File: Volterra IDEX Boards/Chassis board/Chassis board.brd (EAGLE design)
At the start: 102.2 x 54 mm, 29 parts, among them K1 FFC/FPC/34PIN/1MMPITCH/TOPLOCK, K2 FFC/FPC/34PIN/1MMPITCH/TOPLOCK, K3 FFC/FPC/34PIN/1MMPITCH/TOPLOCK, X1 JST-XH-02-PIN-LONG-PAD

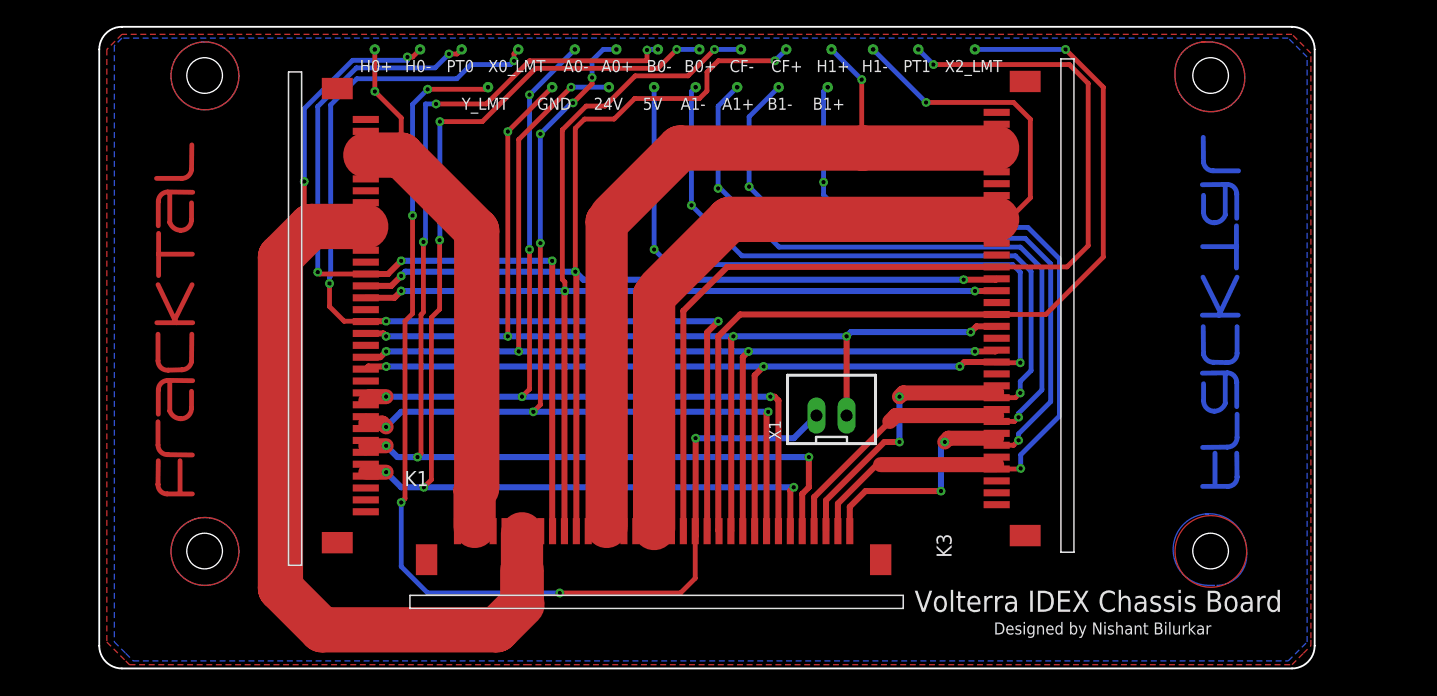
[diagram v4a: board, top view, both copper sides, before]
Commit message: Updated Chassis Board mount holes and re-routing
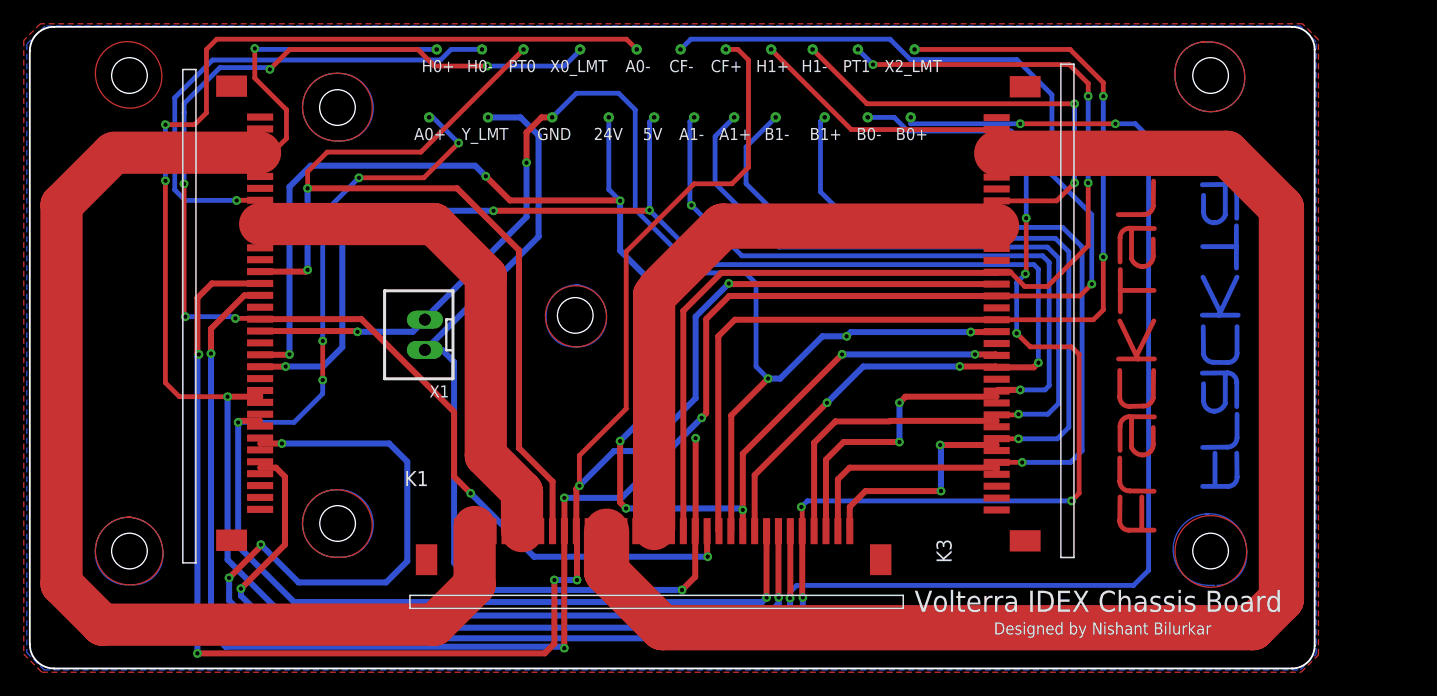
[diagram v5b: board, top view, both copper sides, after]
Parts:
- moved U$2 81.0 mm to (96.5, 27.4)
- moved X1 34.9 mm to (35.0, 31.9), turned to 90 degrees
- moved TP19 18.7 mm to (75.9, 50.2)
- moved TP18 18.6 mm to (72.3, 50.2)
- moved TP20 16.8 mm to (35.4, 50.2)
- moved K2 8.89 mm to (19.1, 35.8)
- moved TP1 5.21 mm to (39.8, 55.9)
- moved TP2 5.21 mm to (43.3, 55.9)
- moved TP21 5.21 mm to (36.0, 55.9)
- moved TP5 5.21 mm to (48.1, 55.9)
- moved TP9 5.21 mm to (52.8, 55.9)
- moved TP10 5.08 mm to (67.6, 55.9)
- moved TP11 5.08 mm to (71.4, 55.9)
- moved TP12 5.08 mm to (76.2, 55.9)
- moved TP22 5.08 mm to (64.1, 55.9)
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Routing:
- net B0-: track 97.1 -> 174.0 mm, vias 6 -> 9
- net CF-: track 105.0 -> 181.1 mm, vias 4 -> 5
- net H0+: track 55.4 -> 128.1 mm
- net H1+: track 78.0 -> 150.7 mm, vias 1 -> 0
- net A0-: track 78.0 -> 145.8 mm, vias 5 -> 4
- net CF+: track 109.2 -> 173.5 mm, vias 4 -> 6
- net B0+: track 97.0 -> 158.5 mm, vias 6 -> 4
- net 24V: track 95.9 -> 123.5 mm, vias 5 -> 8
- net A0+: track 79.7 -> 105.9 mm, vias 7 -> 6
- net X0_LMT: track 86.4 -> 112.2 mm, vias 4 -> 7
- net Y_LMT: track 95.6 -> 80.9 mm, vias 5 -> 2
- net H1-: track 84.5 -> 96.2 mm, vias 1 -> 2
- net GND: track 99.2 -> 109.2 mm, vias 6 -> 5
- net PT0: track 71.0 -> 79.5 mm, vias 4 -> 2
- net X1_LMT: track 78.0 -> 85.9 mm, vias 1 -> 2
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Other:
- board size 102.2 x 54 mm -> 108.1 x 54 mm
